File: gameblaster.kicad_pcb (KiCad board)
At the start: 2 copper layers, 136.7 x 109.8 mm, 67 parts, among them IC1 TEA2025, IC10 74LS138, IC11 74LS08, IC12 74LS14, IC2 SAA1099, IC3 SAA1099, IC4 74LS374, IC5 74LS138, IC6 74LS74, IC7 74LS245, IC8 74LS32, IC9 74LS125, J1 Conn_02x06_Odd_Even

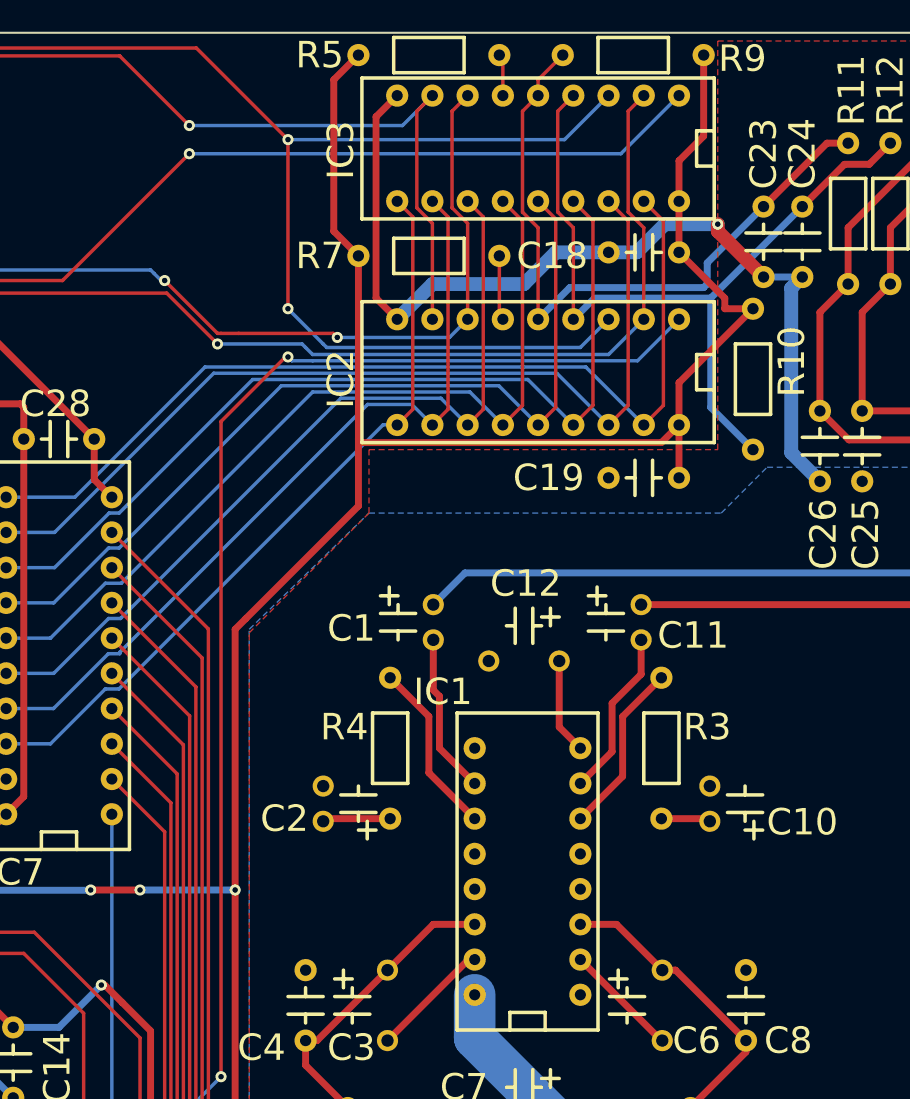
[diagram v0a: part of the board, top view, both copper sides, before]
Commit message: add zener regulator for SAA1099s
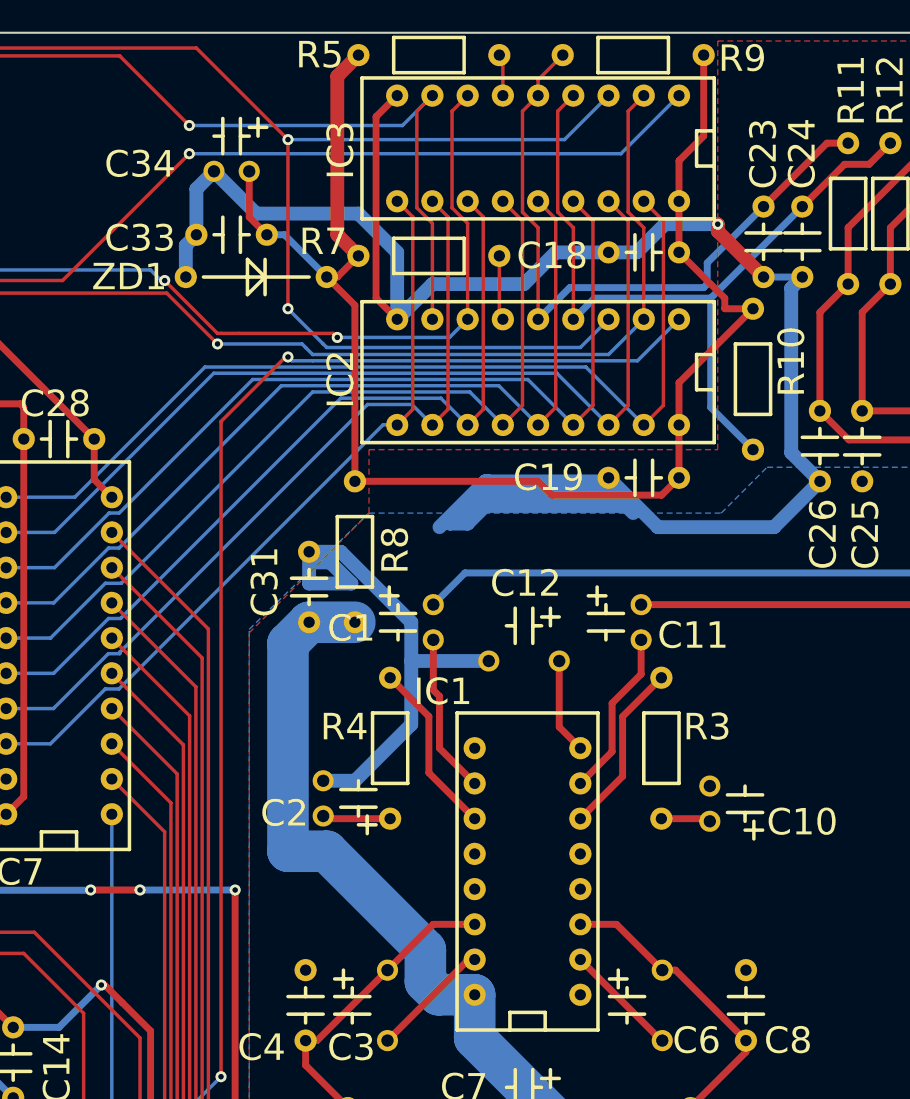
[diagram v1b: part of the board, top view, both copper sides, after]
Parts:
- added C31: 0.1uF, gameblaster:CAPAC200, F.Cu at (138.9, 71.1)
- added C33: 0.1uF, gameblaster:CAPAC200, F.Cu at (135.9, 43.2)
- added C34: 10uF 16V, gameblaster:CAPAP100, F.Cu at (134.6, 38.6)
- added R8: 10K, gameblaster:RESA400, F.Cu at (142.2, 71.1)
- added ZD1: 5.1V, gameblaster:DIOA400, F.Cu at (140.2, 46.2)
- moved C2 0.38 mm to (140.0, 85.1)
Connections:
- C18 pad 2: /VCC -> /+5VD
- C19 pad 1: /VCC -> /+5VD
- IC2 pad 18: /VCC -> /+5VD
- IC3 pad 18: /VCC -> /+5VD
- R10 pad 1: /VCC -> /+5VD
- R5 pad 1: /VCC -> /+5VD
- R7 pad 1: /VCC -> /+5VD
- R9 pad 1: /VCC -> /+5VD
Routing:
- net /AGND: track 117.5 -> 256.0 mm
- net /VCC: track 578.8 -> 452.9 mm
- net /+5VD: track 0.00 -> 106.0 mm
- net /+12V: track 51.7 -> 91.2 mm

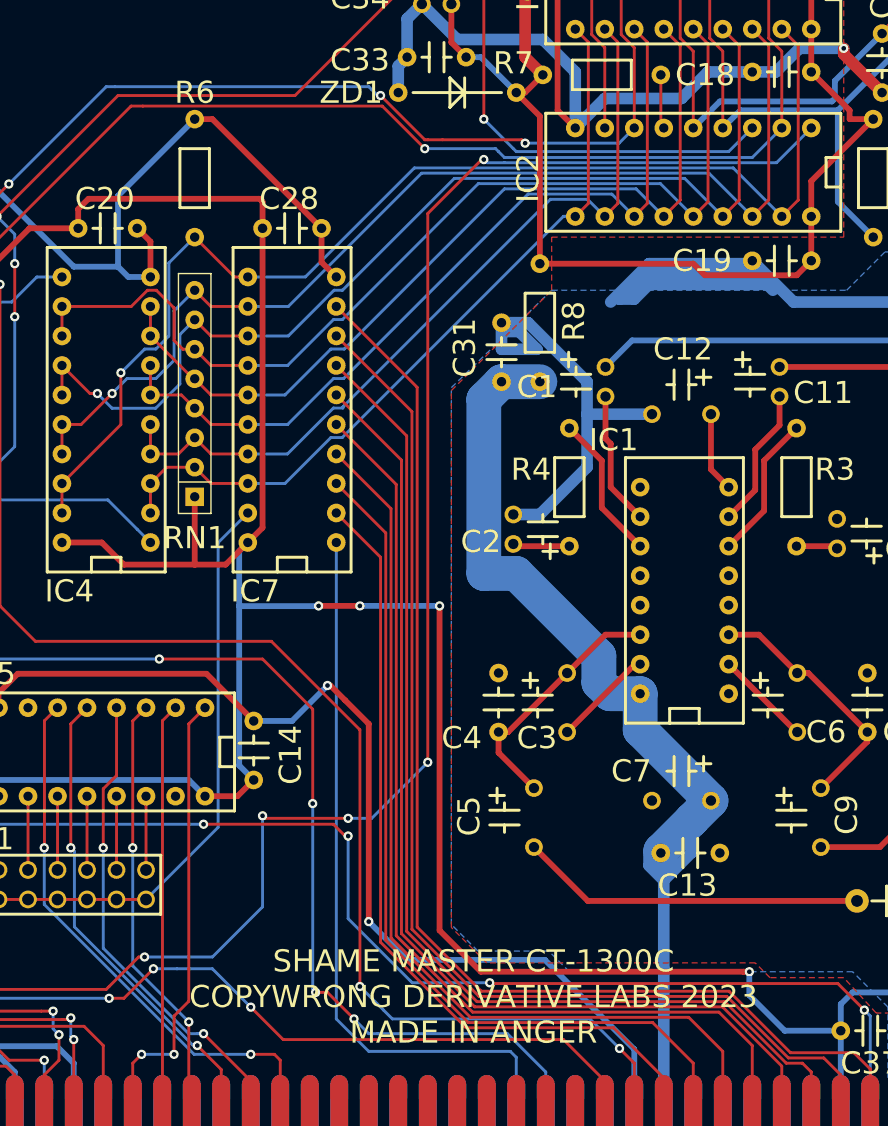
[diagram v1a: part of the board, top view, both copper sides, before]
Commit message: moved R6 because i like the way this looks better
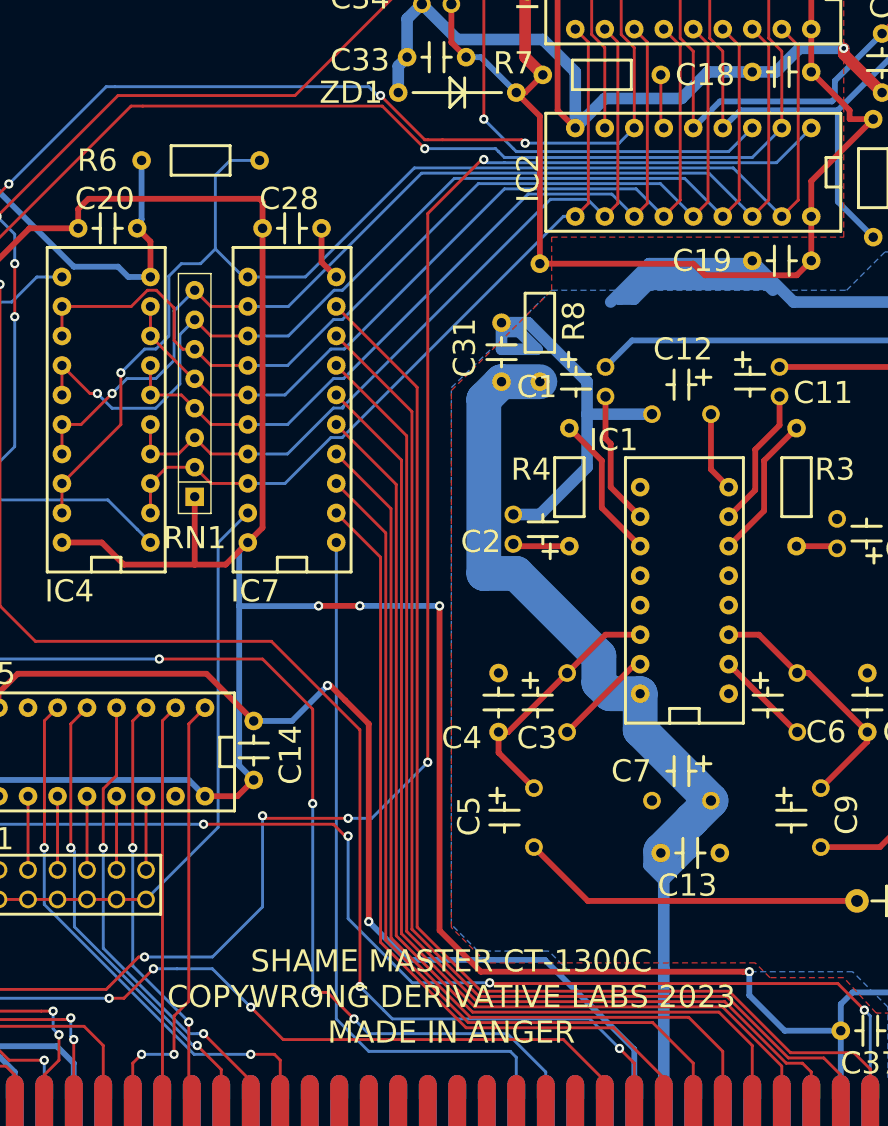
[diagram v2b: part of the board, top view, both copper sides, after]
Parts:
- moved R6 8.65 mm to (118.1, 52.1), turned to 180 degrees
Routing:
- net /GND: track 547.3 -> 523.0 mm
- net /DB7: track 103.9 -> 113.2 mm
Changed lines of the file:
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@@
   )
   (footprint "gameblaster:RESA400" (layer "F.Cu")
-    (at 112.522 58.674 90)
-    (property "Sheetfile" "gameblaster.kicad_sch")
-    (property "Sheetname" "")
-    (attr through_hole)
-    (fp_text reference "R6" (at 12.446 0 180) (layer "F.SilkS")
-      (effects (font (size 1.905 1.905) (thickness 0.254)))
-    )
-    (fp_text value "4.7K" (at 5.08 0 90) (layer "F.Fab")
+    (at 118.11 52.07 180)
+    (property "Sheetfile" "gameblaster.kicad_sch")
+    (property "Sheetname" "")
+    (attr through_hole)
+    (fp_text reference "R6" (at 13.97 0 180) (layer "F.SilkS")
+      (effects (font (size 1.905 1.905) (thickness 0.254)))
+    )
+    (fp_text value "4.7K" (at 5.08 0) (layer "F.Fab")
       (effects (font (size 1 1) (thickness 0.15)))
     )
@@
     (fp_line (start 2.54 -1.27) (end 2.54 1.27) (layer "F.SilkS") (width 0.254))
     (fp_line (start 7.62 1.27) (end 7.62 -1.27) (layer "F.SilkS") (width 0.254))
-    (pad "1" thru_hole circle (at 0 0 90) (size 1.6002 1.6002) (drill 0.8128) (layers *.Cu *.Mask)
+    (pad "1" thru_hole circle (at 0 0 180) (size 1.6002 1.6002) (drill 0.8128) (layers *.Cu *.Mask)
       (net 72 "/DB7") (pintype "passive"))
-    (pad "2" thru_hole circle (at 10.16 0 90) (size 1.6002 1.6002) (drill 0.8128) (layers *.Cu *.Mask)
+    (pad "2" thru_hole circle (at 10.16 0 180) (size 1.6002 1.6002) (drill 0.8128) (layers *.Cu *.Mask)
       (net 75 "/GND") (pintype "passive"))
     (model "${KICAD6_3DMODEL_DIR}/Resistor_THT.3dshapes/R_Axial_DIN0207_L6.3mm_D2.5mm_P10.16mm_Horizontal.step"
@@
     (effects (font (size 0.9525 0.9525) (thickness 0.127)) (justify left mirror))
   )
-  (gr_text "SHAME MASTER CT-1300C\nCOPYWRONG DERIVATIVE LABS 2023\nMADE IN ANGER" (at 136.525 124.079) (layer "F.SilkS")
+  (gr_text "SHAME MASTER CT-1300C\nCOPYWRONG DERIVATIVE LABS 2023\nMADE IN ANGER" (at 134.62 124.079) (layer "F.SilkS")
     (effects (font (size 1.905 1.905) (thickness 0.254)))
   )
@@
   (segment (start 164.483 55.481) (end 164.483 42.182) (width 0.25) (layer "F.Cu") (net 72))
   (segment (start 106.16756 74.80744) (end 106.16756 70.353842) (width 0.25) (layer "F.Cu") (net 72))
-  (segment (start 115.951 62.103) (end 112.522 58.674) (width 0.25) (layer "F.Cu") (net 72))
   (segment (start 164.483 42.182) (end 163.068 40.767) (width 0.25) (layer "F.Cu") (net 72))
   (segment (start 163.068 56.896) (end 164.483 55.481) (width 0.25) (layer "F.Cu") (net 72))
   (segment (start 101.092 79.883) (end 106.16756 74.80744) (width 0.25) (layer "F.Cu") (net 72))
-  (segment (start 117.094 62.103) (end 115.951 62.103) (width 0.25) (layer "F.Cu") (net 72))
   (segment (start 101.092 82.423) (end 101.092 79.883) (width 0.25) (layer "F.Cu") (net 72))
   (via (at 106.16756 70.353842) (size 0.8) (drill 0.4) (layers "F.Cu" "B.Cu") (net 72))
+  (segment (start 110.294 67.191991) (end 110.294 62.034) (width 0.25) (layer "B.Cu") (net 72))
+  (segment (start 158.888 52.716) (end 163.068 56.896) (width 0.25) (layer "B.Cu") (net 72))
+  (segment (start 106.16756 70.353842) (end 108.213402 68.308) (width 0.25) (layer "B.Cu") (net 72))
+  (segment (start 111.368 60.96) (end 113.03 60.96) (width 0.25) (layer "B.Cu") (net 72))
+  (segment (start 114.3 53.34) (end 115.57 52.07) (width 0.25) (layer "B.Cu") (net 72))
   (segment (start 109.177991 68.308) (end 110.294 67.191991) (width 0.25) (layer "B.Cu") (net 72))
-  (segment (start 158.888 52.716) (end 163.068 56.896) (width 0.25) (layer "B.Cu") (net 72))
-  (segment (start 108.213402 68.308) (end 109.177991 68.308) (width 0.25) (layer "B.Cu") (net 72))
-  (segment (start 110.294 67.191991) (end 110.294 60.902) (width 0.25) (layer "B.Cu") (net 72))
-  (segment (start 106.16756 70.353842) (end 108.213402 68.308) (width 0.25) (layer "B.Cu") (net 72))
+  (segment (start 116.967 62.23) (end 117.094 62.103) (width 0.25) (layer "B.Cu") (net 72))
+  (segment (start 110.294 62.034) (end 111.368 60.96) (width 0.25) (layer "B.Cu") (net 72))
+  (segment (start 114.3 59.69) (end 114.3 53.34) (width 0.25) (layer "B.Cu") (net 72))
   (segment (start 131.434 52.716) (end 158.888 52.716) (width 0.25) (layer "B.Cu") (net 72))
   (segment (start 122.047 62.103) (end 131.434 52.716) (width 0.25) (layer "B.Cu") (net 72))
-  (segment (start 110.294 60.902) (end 112.522 58.674) (width 0.25) (layer "B.Cu") (net 72))
+  (segment (start 113.03 60.96) (end 114.3 59.69) (width 0.25) (layer "B.Cu") (net 72))
+  (segment (start 116.84 62.23) (end 116.967 62.23) (width 0.25) (layer "B.Cu") (net 72))
   (segment (start 117.094 62.103) (end 122.047 62.103) (width 0.25) (layer "B.Cu") (net 72))
+  (segment (start 108.213402 68.308) (end 109.177991 68.308) (width 0.25) (layer "B.Cu") (net 72))
+  (segment (start 114.3 59.69) (end 116.84 62.23) (width 0.25) (layer "B.Cu") (net 72))
+  (segment (start 115.57 52.07) (end 118.11 52.07) (width 0.25) (layer "B.Cu") (net 72))
   (segment (start 121.158 46.482) (end 130.302 37.338) (width 0.25) (layer "F.Cu") (net 73))
   (segment (start 78.867 123.317) (end 78.867 117.287991) (width 0.25) (layer "F.Cu") (net 73))
@@
   (segment (start 125.476 98.552) (end 124.201701 97.277701) (width 0.5) (layer "F.Cu") (net 75))
   (segment (start 73.152 54.102) (end 74.93 54.102) (width 0.5) (layer "F.Cu") (net 75))
-  (segment (start 123.444 57.912) (end 114.046 48.514) (width 0.5) (layer "F.Cu") (net 75))
   (segment (start 127.508 117.602) (end 127.508 100.584) (width 0.5) (layer "F.Cu") (net 75))
   (segment (start 75.692 69.596) (end 74.93 70.358) (width 0.5) (layer "F.Cu") (net 75))
   (segment (start 95.631 99.187) (end 95.631 97.917) (width 0.5) (layer "F.Cu") (net 75))
   (segment (start 124.201701 97.277701) (end 123.956299 97.277701) (width 0.5) (layer "F.Cu") (net 75))
-  (segment (start 114.046 48.514) (end 112.522 48.514) (width 0.5) (layer "F.Cu") (net 75))
   (segment (start 78.359 66.167) (end 75.692 68.834) (width 0.5) (layer "F.Cu") (net 75))
   (segment (start 74.93 54.102) (end 75.692 54.864) (width 0.5) (layer "F.Cu") (net 75))
@@
   (segment (start 65.913 82.677) (end 63.627 82.677) (width 0.5) (layer "B.Cu") (net 75))
   (segment (start 84.201 66.167) (end 85.344 67.31) (width 0.5) (layer "B.Cu") (net 75))
-  (segment (start 105.918 55.118) (end 105.918 61.214) (width 0.5) (layer "B.Cu") (net 75))
   (segment (start 85.598 100.33) (end 86.741 99.187) (width 0.5) (layer "B.Cu") (net 75))
   (segment (start 80.899 66.167) (end 84.201 66.167) (width 0.5) (layer "B.Cu") (net 75))
@@
   (segment (start 63.5 82.55) (end 63.5 66.04) (width 0.5) (layer "B.Cu") (net 75))
   (segment (start 65.659 68.707) (end 68.199 71.247) (width 0.5) (layer "B.Cu") (net 75))
-  (segment (start 112.522 48.514) (end 105.918 55.118) (width 0.5) (layer "B.Cu") (net 75))
   (segment (start 106.807 62.103) (end 108.712 62.103) (width 0.5) (layer "B.Cu") (net 75))
   (segment (start 81.788 128.3335) (end 83.2485 129.794) (width 0.5) (layer "B.Cu") (net 75))
@@
   (segment (start 81.788 128.3335) (end 66.6115 128.3335) (width 0.5) (layer "B.Cu") (net 75))
   (segment (start 85.344 31.242) (end 85.344 34.036) (width 0.5) (layer "B.Cu") (net 75))
+  (segment (start 107.95 57.15) (end 107.95 52.07) (width 0.5) (layer "B.Cu") (net 75))
   (segment (start 63.627 66.167) (end 63.5 66.04) (width 0.5) (layer "B.Cu") (net 75))
   (segment (start 83.2485 129.794) (end 84.836 129.794) (width 0.5) (layer "B.Cu") (net 75))
+  (segment (start 107.569 57.912) (end 107.569 57.531) (width 0.5) (layer "B.Cu") (net 75))
   (segment (start 87.122 40.132) (end 87.122 35.814) (width 0.5) (layer "B.Cu") (net 75))
   (segment (start 91.694 50.8) (end 85.344 50.8) (width 0.5) (layer "B.Cu") (net 75))
@@
   (segment (start 87.122 35.814) (end 85.344 34.036) (width 0.5) (layer "B.Cu") (net 75))
   (segment (start 76.2 102.108) (end 76.2 99.187) (width 0.5) (layer "B.Cu") (net 75))
+  (segment (start 107.569 57.531) (end 107.95 57.15) (width 0.5) (layer "B.Cu") (net 75))
   (segment (start 65.659 66.167) (end 63.627 66.167) (width 0.5) (layer "B.Cu") (net 75))
   (segment (start 63.5 49.53) (end 63.5 34.036) (width 0.5) (layer "B.Cu") (net 75))

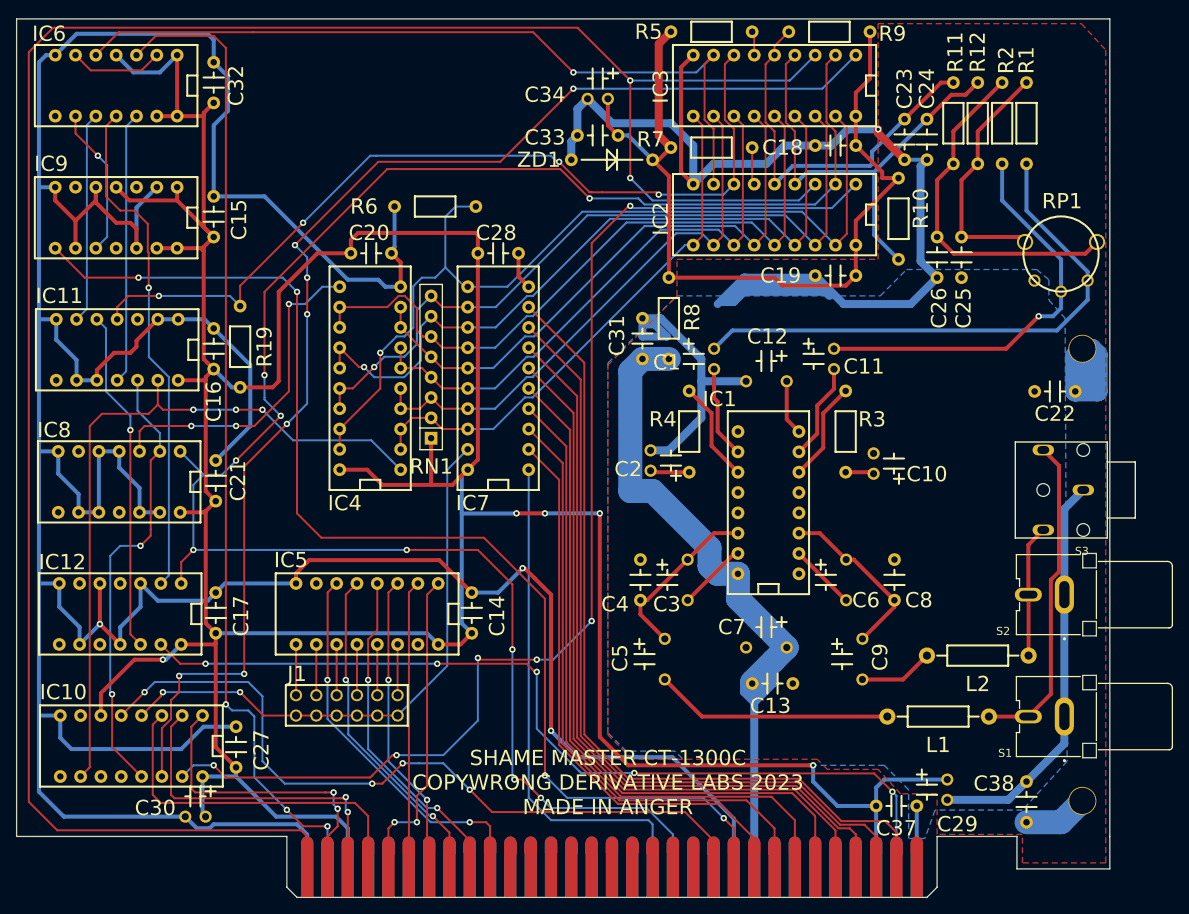
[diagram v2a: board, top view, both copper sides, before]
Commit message: added some 3d crap, moved some components around to fit
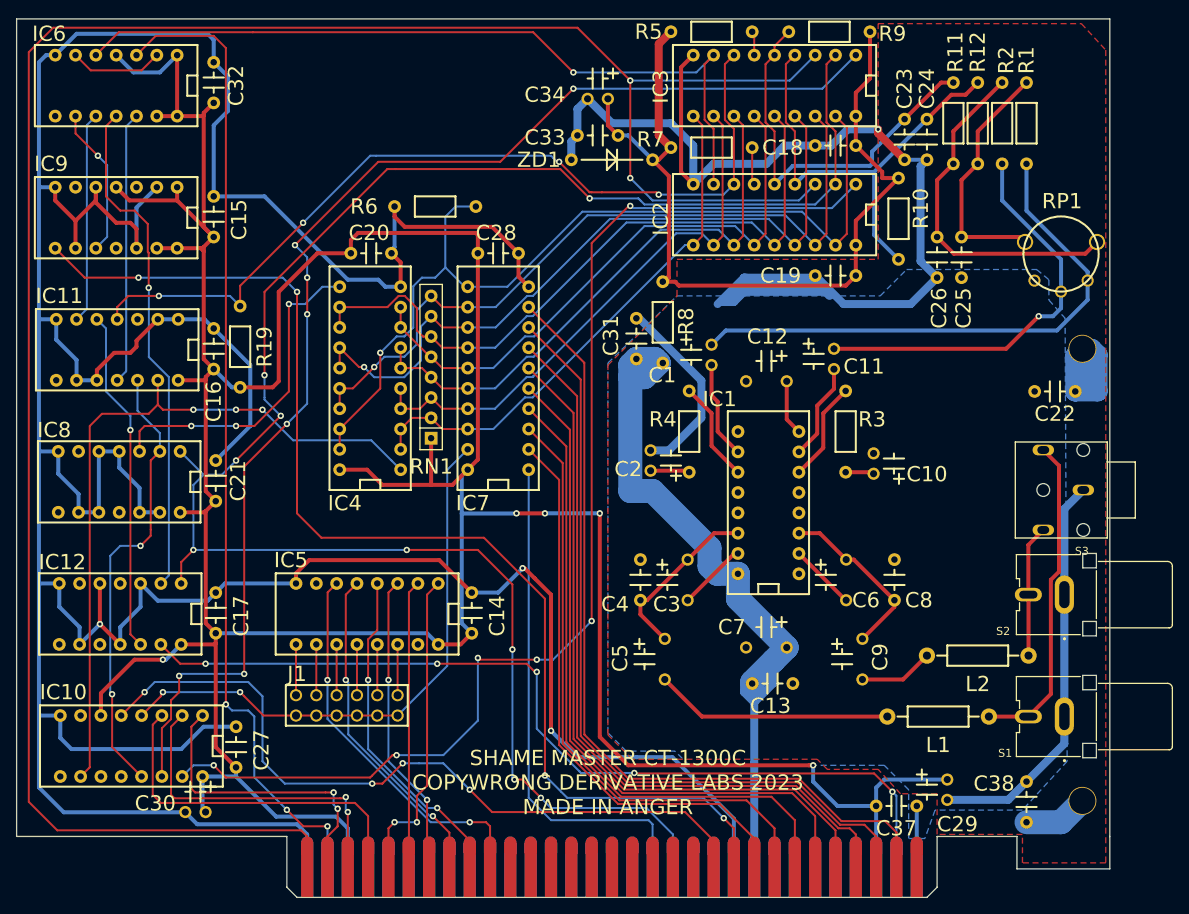
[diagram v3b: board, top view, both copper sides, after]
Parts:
- moved R8 0.92 mm to (141.5, 71.6)
- moved C31 0.76 mm to (138.2, 71.1)
- moved C1 0.60 mm to (147.6, 69.3)
- moved C30 0.57 mm to (84.3, 127.8)
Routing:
- net /GND: track 523.0 -> 541.0 mm
- net /AGND: track 256.0 -> 241.1 mm
- net /+12V: track 91.2 -> 93.9 mm
- net /+5VD: track 106.0 -> 107.6 mm
- net /CHASSIS: track 30.5 -> 29.4 mm
- net Net-(C1-Pad2): track 11.6 -> 12.2 mm
- net /VCC: track 452.9 -> 452.3 mm
